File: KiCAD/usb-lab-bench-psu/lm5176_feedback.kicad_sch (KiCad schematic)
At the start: 17 parts, among them J10 Conn_01x03, U10 MCP602, U11 MCP4728

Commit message: restructured schematics to better show individual boards
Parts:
- renumbered J10 to J25, R62 to R100, R61 to R101, U10 to U17
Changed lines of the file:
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@@
 		(instances
 			(project "usb-lab-bench-psu"
-				(path "/63928bc9-e618-488a-a687-c6d5597f31d9/ef40a3f9-2fe8-4f01-b5d3-ede47a6064fc/25196ac8-3e62-4aeb-a723-5f08504eebf8"
-					(reference "R51")
+				(path "/63928bc9-e618-488a-a687-c6d5597f31d9/a793a91b-724b-4226-ba64-0dd946e3992c/7f670fa9-133d-4e8e-a284-e2ede26f8135/25196ac8-3e62-4aeb-a723-5f08504eebf8"
+					(reference "R92")
 					(unit 1)
 				)
@@
 		(dnp no)
 		(fields_autoplaced yes)
-		(property "Reference" "U10"
+		(property "Reference" "U17"
 			(at 86.36 59.6899 0)
 			(effects
@@
 		)
 		(instances
-			(project ""
-				(path "/63928bc9-e618-488a-a687-c6d5597f31d9/ef40a3f9-2fe8-4f01-b5d3-ede47a6064fc/25196ac8-3e62-4aeb-a723-5f08504eebf8"
-					(reference "U10")
+			(project "usb-lab-bench-psu"
+				(path "/63928bc9-e618-488a-a687-c6d5597f31d9/a793a91b-724b-4226-ba64-0dd946e3992c/7f670fa9-133d-4e8e-a284-e2ede26f8135/25196ac8-3e62-4aeb-a723-5f08504eebf8"
+					(reference "U17")
 					(unit 3)
 				)
@@
 		(instances
 			(project "usb-lab-bench-psu"
-				(path "/63928bc9-e618-488a-a687-c6d5597f31d9/ef40a3f9-2fe8-4f01-b5d3-ede47a6064fc/25196ac8-3e62-4aeb-a723-5f08504eebf8"
-					(reference "R57")
+				(path "/63928bc9-e618-488a-a687-c6d5597f31d9/a793a91b-724b-4226-ba64-0dd946e3992c/7f670fa9-133d-4e8e-a284-e2ede26f8135/25196ac8-3e62-4aeb-a723-5f08504eebf8"
+					(reference "R95")
 					(unit 1)
 				)
@@
 		(dnp no)
 		(fields_autoplaced yes)
-		(property "Reference" "J10"
+		(property "Reference" "J25"
 			(at 24.13 86.36 0)
 			(effects
@@
 		)
 		(instances
-			(project ""
-				(path "/63928bc9-e618-488a-a687-c6d5597f31d9/ef40a3f9-2fe8-4f01-b5d3-ede47a6064fc/25196ac8-3e62-4aeb-a723-5f08504eebf8"
-					(reference "J10")
+			(project "usb-lab-bench-psu"
+				(path "/63928bc9-e618-488a-a687-c6d5597f31d9/a793a91b-724b-4226-ba64-0dd946e3992c/7f670fa9-133d-4e8e-a284-e2ede26f8135/25196ac8-3e62-4aeb-a723-5f08504eebf8"
+					(reference "J25")
 					(unit 1)
 				)
@@
 		(dnp no)
 		(fields_autoplaced yes)
-		(property "Reference" "R61"
+		(property "Reference" "R101"
 			(at 191.77 60.96 90)
 			(effects
@@
 		)
 		(instances
-			(project ""
-				(path "/63928bc9-e618-488a-a687-c6d5597f31d9/ef40a3f9-2fe8-4f01-b5d3-ede47a6064fc/25196ac8-3e62-4aeb-a723-5f08504eebf8"
-					(reference "R61")
+			(project "usb-lab-bench-psu"
+				(path "/63928bc9-e618-488a-a687-c6d5597f31d9/a793a91b-724b-4226-ba64-0dd946e3992c/7f670fa9-133d-4e8e-a284-e2ede26f8135/25196ac8-3e62-4aeb-a723-5f08504eebf8"
+					(reference "R101")
 					(unit 1)
 				)
@@
 		(instances
 			(project "usb-lab-bench-psu"
-				(path "/63928bc9-e618-488a-a687-c6d5597f31d9/ef40a3f9-2fe8-4f01-b5d3-ede47a6064fc/25196ac8-3e62-4aeb-a723-5f08504eebf8"
-					(reference "R52")
+				(path "/63928bc9-e618-488a-a687-c6d5597f31d9/a793a91b-724b-4226-ba64-0dd946e3992c/7f670fa9-133d-4e8e-a284-e2ede26f8135/25196ac8-3e62-4aeb-a723-5f08504eebf8"
+					(reference "R93")
 					(unit 1)
 				)
@@
 		(instances
 			(project "usb-lab-bench-psu"
-				(path "/63928bc9-e618-488a-a687-c6d5597f31d9/ef40a3f9-2fe8-4f01-b5d3-ede47a6064fc/25196ac8-3e62-4aeb-a723-5f08504eebf8"
-					(reference "TP10")
+				(path "/63928bc9-e618-488a-a687-c6d5597f31d9/a793a91b-724b-4226-ba64-0dd946e3992c/7f670fa9-133d-4e8e-a284-e2ede26f8135/25196ac8-3e62-4aeb-a723-5f08504eebf8"
+					(reference "TP17")
 					(unit 1)
 				)
@@
 		(on_board yes)
 		(dnp no)
-		(property "Reference" "U10"
+		(property "Reference" "U17"
 			(at 199.39 91.44 0)
 			(effects
@@
 		)
 		(instances
-			(project ""
-				(path "/63928bc9-e618-488a-a687-c6d5597f31d9/ef40a3f9-2fe8-4f01-b5d3-ede47a6064fc/25196ac8-3e62-4aeb-a723-5f08504eebf8"
-					(reference "U10")
+			(project "usb-lab-bench-psu"
+				(path "/63928bc9-e618-488a-a687-c6d5597f31d9/a793a91b-724b-4226-ba64-0dd946e3992c/7f670fa9-133d-4e8e-a284-e2ede26f8135/25196ac8-3e62-4aeb-a723-5f08504eebf8"
+					(reference "U17")
 					(unit 1)
 				)
@@
 		(dnp no)
 		(fields_autoplaced yes)
-		(property "Reference" "U10"
+		(property "Reference" "U17"
 			(at 233.68 73.66 0)
 			(effects
@@
 		)
 		(instances
-			(project ""
-				(path "/63928bc9-e618-488a-a687-c6d5597f31d9/ef40a3f9-2fe8-4f01-b5d3-ede47a6064fc/25196ac8-3e62-4aeb-a723-5f08504eebf8"
-					(reference "U10")
+			(project "usb-lab-bench-psu"
+				(path "/63928bc9-e618-488a-a687-c6d5597f31d9/a793a91b-724b-4226-ba64-0dd946e3992c/7f670fa9-133d-4e8e-a284-e2ede26f8135/25196ac8-3e62-4aeb-a723-5f08504eebf8"
+					(reference "U17")
 					(unit 2)
 				)
@@
 		(instances
 			(project "usb-lab-bench-psu"
-				(path "/63928bc9-e618-488a-a687-c6d5597f31d9/ef40a3f9-2fe8-4f01-b5d3-ede47a6064fc/25196ac8-3e62-4aeb-a723-5f08504eebf8"
-					(reference "R58")
+				(path "/63928bc9-e618-488a-a687-c6d5597f31d9/a793a91b-724b-4226-ba64-0dd946e3992c/7f670fa9-133d-4e8e-a284-e2ede26f8135/25196ac8-3e62-4aeb-a723-5f08504eebf8"
+					(reference "R96")
 					(unit 1)
 				)
@@
 		(dnp no)
 		(fields_autoplaced yes)
-		(property "Reference" "R62"
+		(property "Reference" "R100"
 			(at 179.07 68.5799 0)
 			(effects
@@
 		)
 		(instances
-			(project ""
-				(path "/63928bc9-e618-488a-a687-c6d5597f31d9/ef40a3f9-2fe8-4f01-b5d3-ede47a6064fc/25196ac8-3e62-4aeb-a723-5f08504eebf8"
-					(reference "R62")
+			(project "usb-lab-bench-psu"
+				(path "/63928bc9-e618-488a-a687-c6d5597f31d9/a793a91b-724b-4226-ba64-0dd946e3992c/7f670fa9-133d-4e8e-a284-e2ede26f8135/25196ac8-3e62-4aeb-a723-5f08504eebf8"
+					(reference "R100")
 					(unit 1)
 				)
@@
 		(instances
 			(project "usb-lab-bench-psu"
-				(path "/63928bc9-e618-488a-a687-c6d5597f31d9/ef40a3f9-2fe8-4f01-b5d3-ede47a6064fc/25196ac8-3e62-4aeb-a723-5f08504eebf8"
-					(reference "R60")
+				(path "/63928bc9-e618-488a-a687-c6d5597f31d9/a793a91b-724b-4226-ba64-0dd946e3992c/7f670fa9-133d-4e8e-a284-e2ede26f8135/25196ac8-3e62-4aeb-a723-5f08504eebf8"
+					(reference "R99")
 					(unit 1)
 				)
@@
 		(instances
 			(project "usb-lab-bench-psu"
-				(path "/63928bc9-e618-488a-a687-c6d5597f31d9/ef40a3f9-2fe8-4f01-b5d3-ede47a6064fc/25196ac8-3e62-4aeb-a723-5f08504eebf8"
-					(reference "R64")
+				(path "/63928bc9-e618-488a-a687-c6d5597f31d9/a793a91b-724b-4226-ba64-0dd946e3992c/7f670fa9-133d-4e8e-a284-e2ede26f8135/25196ac8-3e62-4aeb-a723-5f08504eebf8"
+					(reference "R98")
 					(unit 1)
 				)
@@
 		(instances
 			(project "usb-lab-bench-psu"
-				(path "/63928bc9-e618-488a-a687-c6d5597f31d9/ef40a3f9-2fe8-4f01-b5d3-ede47a6064fc/25196ac8-3e62-4aeb-a723-5f08504eebf8"
-					(reference "R63")
+				(path "/63928bc9-e618-488a-a687-c6d5597f31d9/a793a91b-724b-4226-ba64-0dd946e3992c/7f670fa9-133d-4e8e-a284-e2ede26f8135/25196ac8-3e62-4aeb-a723-5f08504eebf8"
+					(reference "R97")
 					(unit 1)
 				)
@@
 		(instances
 			(project "usb-lab-bench-psu"
-				(path "/63928bc9-e618-488a-a687-c6d5597f31d9/ef40a3f9-2fe8-4f01-b5d3-ede47a6064fc/25196ac8-3e62-4aeb-a723-5f08504eebf8"
-					(reference "R56")
+				(path "/63928bc9-e618-488a-a687-c6d5597f31d9/a793a91b-724b-4226-ba64-0dd946e3992c/7f670fa9-133d-4e8e-a284-e2ede26f8135/25196ac8-3e62-4aeb-a723-5f08504eebf8"
+					(reference "R94")
 					(unit 1)
 				)
@@
 		(instances
 			(project "usb-lab-bench-psu"
-				(path "/63928bc9-e618-488a-a687-c6d5597f31d9/ef40a3f9-2fe8-4f01-b5d3-ede47a6064fc/25196ac8-3e62-4aeb-a723-5f08504eebf8"
-					(reference "TP11")
+				(path "/63928bc9-e618-488a-a687-c6d5597f31d9/a793a91b-724b-4226-ba64-0dd946e3992c/7f670fa9-133d-4e8e-a284-e2ede26f8135/25196ac8-3e62-4aeb-a723-5f08504eebf8"
+					(reference "TP18")
 					(unit 1)
 				)
@@
 		(instances
 			(project "usb-lab-bench-psu"
-				(path "/63928bc9-e618-488a-a687-c6d5597f31d9/ef40a3f9-2fe8-4f01-b5d3-ede47a6064fc/25196ac8-3e62-4aeb-a723-5f08504eebf8"
-					(reference "TP12")
+				(path "/63928bc9-e618-488a-a687-c6d5597f31d9/a793a91b-724b-4226-ba64-0dd946e3992c/7f670fa9-133d-4e8e-a284-e2ede26f8135/25196ac8-3e62-4aeb-a723-5f08504eebf8"
+					(reference "TP16")
 					(unit 1)
 				)
@@
 		(instances
 			(project "usb-lab-bench-psu"
-				(path "/63928bc9-e618-488a-a687-c6d5597f31d9/ef40a3f9-2fe8-4f01-b5d3-ede47a6064fc/25196ac8-3e62-4aeb-a723-5f08504eebf8"
-					(reference "R59")
+				(path "/63928bc9-e618-488a-a687-c6d5597f31d9/a793a91b-724b-4226-ba64-0dd946e3992c/7f670fa9-133d-4e8e-a284-e2ede26f8135/25196ac8-3e62-4aeb-a723-5f08504eebf8"
+					(reference "R91")
 					(unit 1)
 				)
@@
 		(instances
 			(project "usb-lab-bench-psu"
-				(path "/63928bc9-e618-488a-a687-c6d5597f31d9/ef40a3f9-2fe8-4f01-b5d3-ede47a6064fc/25196ac8-3e62-4aeb-a723-5f08504eebf8"
-					(reference "U11")
-					(unit 1)
-				)
+				(path "/63928bc9-e618-488a-a687-c6d5597f31d9/a793a91b-724b-4226-ba64-0dd946e3992c/7f670fa9-133d-4e8e-a284-e2ede26f8135/25196ac8-3e62-4aeb-a723-5f08504eebf8"
+					(reference "U16")
+					(unit 1)
+				)

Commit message: updated spi for display
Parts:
- renumbered R59 to R91, R51 to R92, R52 to R93, R56 to R94, R57 to R95, R58 to R96, R63 to R97, R64 to R98, R60 to R99, TP12 to TP16, TP10 to TP17, TP11 to TP18, U11 to U16
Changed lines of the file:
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@@
 		(on_board yes)
 		(dnp no)
-		(property "Reference" "R51"
+		(property "Reference" "R92"
 			(at 41.656 81.28 0)
 			(effects
@@
 		(on_board yes)
 		(dnp no)
-		(property "Reference" "R57"
+		(property "Reference" "R95"
 			(at 129.54 82.55 90)
 			(effects
@@
 		(dnp no)
 		(fields_autoplaced yes)
-		(property "Reference" "R52"
+		(property "Reference" "R93"
 			(at 53.34 81.2799 0)
 			(effects
@@
 		(dnp no)
 		(fields_autoplaced yes)
-		(property "Reference" "TP10"
+		(property "Reference" "TP17"
 			(at 135.89 79.2479 0)
 			(effects
@@
 		(on_board yes)
 		(dnp no)
-		(property "Reference" "R58"
+		(property "Reference" "R96"
 			(at 129.54 97.79 90)
 			(effects
@@
 		(dnp no)
 		(fields_autoplaced yes)
-		(property "Reference" "R60"
+		(property "Reference" "R99"
 			(at 170.18 41.91 90)
 			(effects
@@
 		(dnp no)
 		(fields_autoplaced yes)
-		(property "Reference" "R64"
+		(property "Reference" "R98"
 			(at 167.64 88.8999 0)
 			(effects
@@
 		(dnp no)
 		(fields_autoplaced yes)
-		(property "Reference" "R63"
+		(property "Reference" "R97"
 			(at 167.64 68.5799 0)
 			(effects
@@
 		(on_board yes)
 		(dnp no)
-		(property "Reference" "R56"
+		(property "Reference" "R94"
 			(at 116.84 96.52 90)
 			(effects
@@
 		(dnp no)
 		(fields_autoplaced yes)
-		(property "Reference" "TP11"
+		(property "Reference" "TP18"
 			(at 135.89 103.3779 0)
 			(effects
@@
 		(on_board yes)
 		(dnp no)
-		(property "Reference" "TP12"
+		(property "Reference" "TP16"
 			(at 90.932 77.216 0)
 			(effects
@@
 		(on_board yes)
 		(dnp no)
-		(property "Reference" "R59"
+		(property "Reference" "R91"
 			(at 27.686 82.55 0)
 			(effects
@@
 		(dnp no)
 		(fields_autoplaced yes)
-		(property "Reference" "U11"
+		(property "Reference" "U16"
 			(at 75.8541 82.55 0)
 			(effects

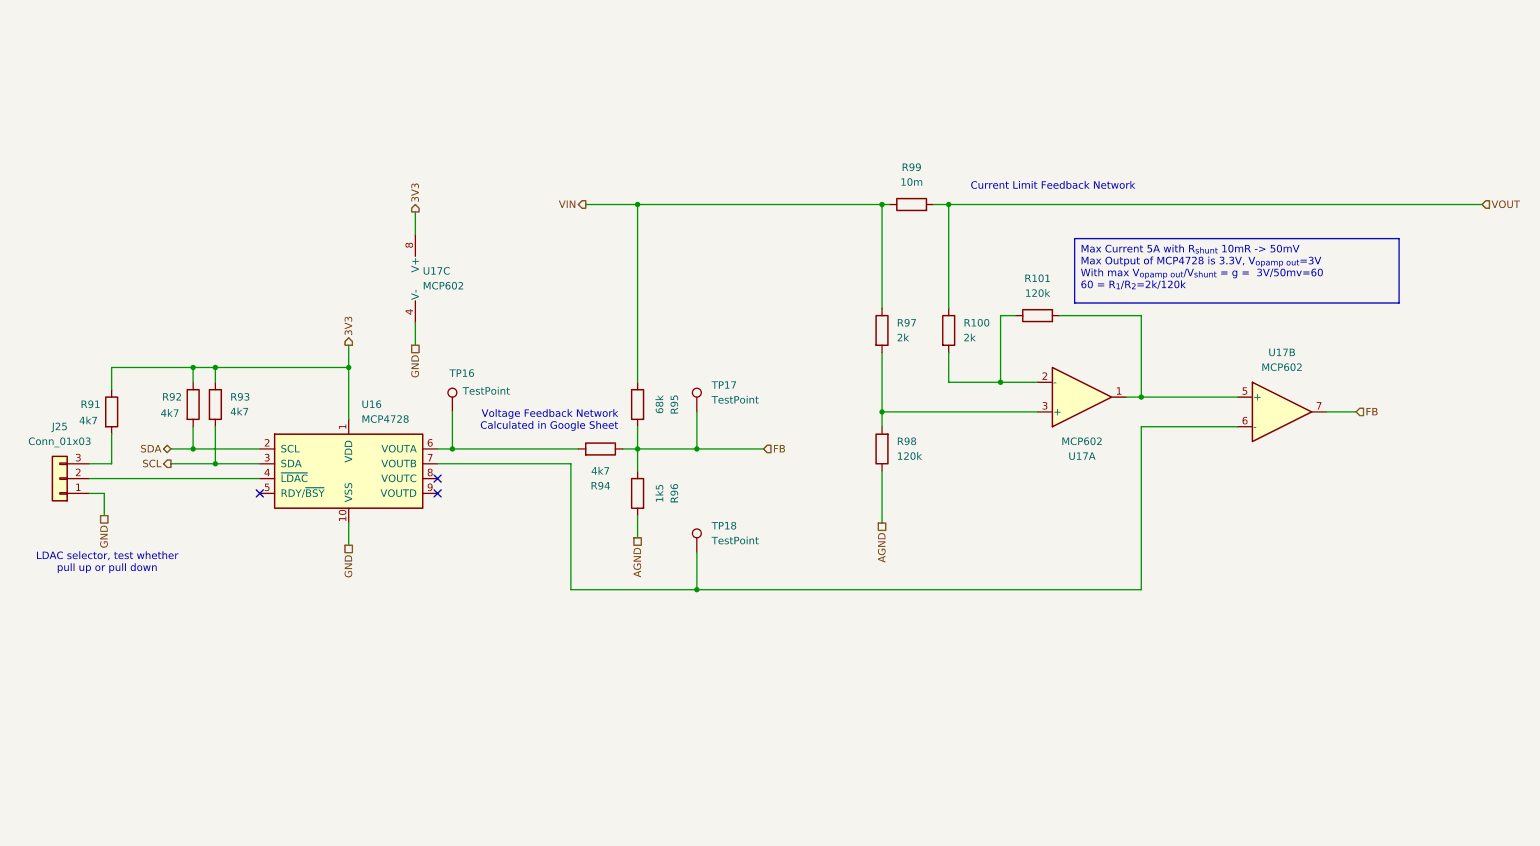
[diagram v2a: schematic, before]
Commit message: added current limiting circuit for USB PD sink, added 2nd buck converter
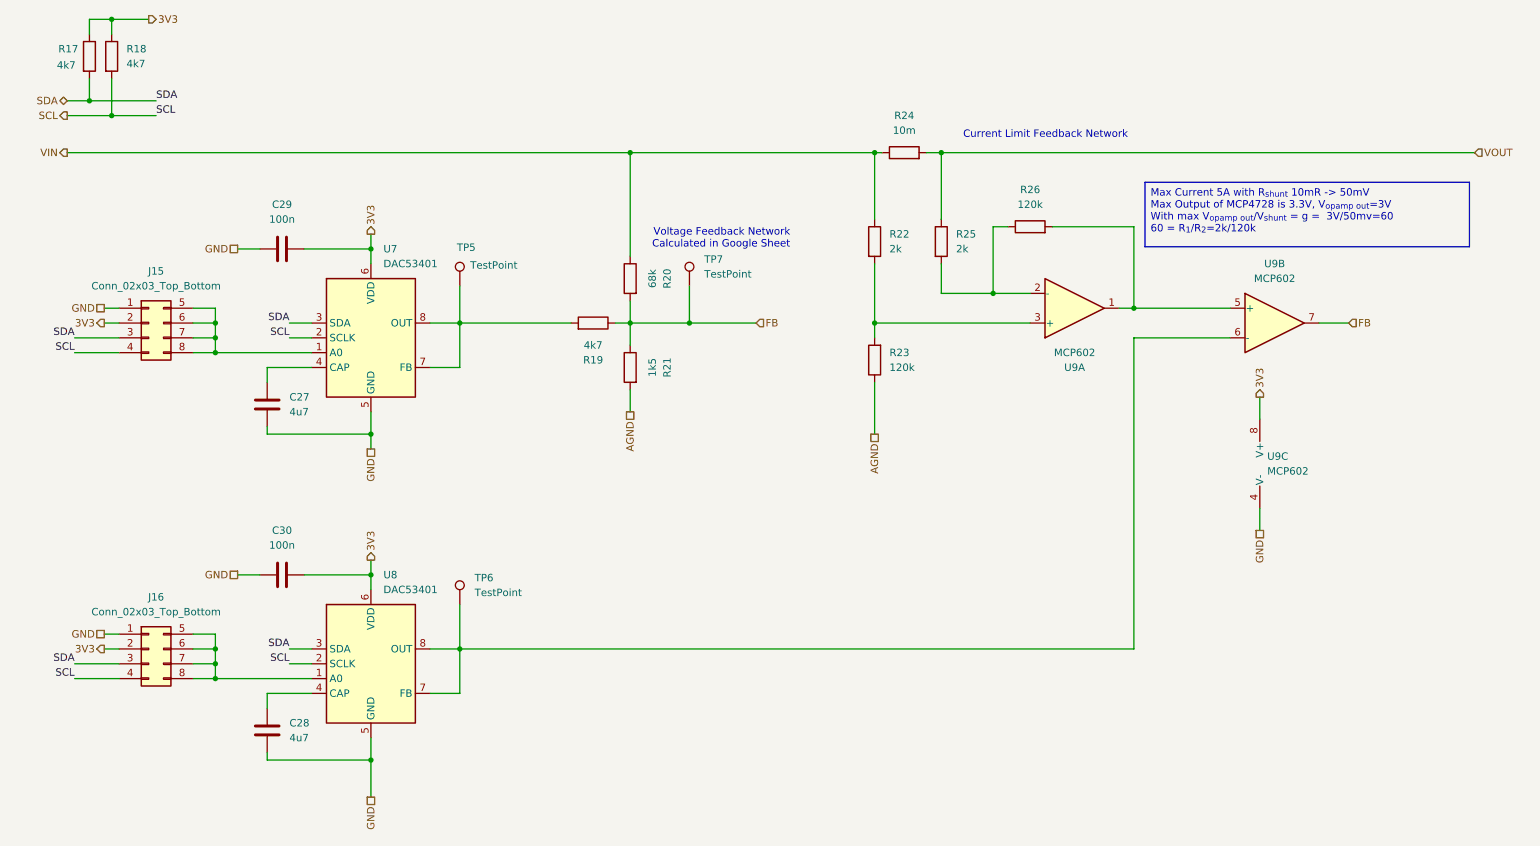
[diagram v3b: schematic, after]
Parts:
- removed J25: Conn_01x03, symbol Connector_Generic:Conn_01x03
- removed R91: 4k7, symbol Device:R
- removed U16: MCP4728, Package_SO:MSOP-10_3x3mm_P0.5mm, symbol Analog_DAC:MCP4728
- added C27, C28: 4u7, symbol Device:C
- added C29, C30: 100n, symbol Device:C
- added J15, J16: Conn_02x03_Top_Bottom, symbol Connector_Generic:Conn_02x04_Top_Bottom
- added U7, U8: DAC53401, Package_SON:WSON-8-1EP_2x2mm_P0.5mm_EP0.9x1.6mm, symbol Prj_DAC:DAC53401
- renumbered R92 to R17, R93 to R18, R94 to R19, R95 to R20, R96 to R21, R97 to R22, R98 to R23, R99 to R24, R100 to R25, R101 to R26, TP16 to TP5, TP18 to TP6, TP17 to TP7, U17 to U9
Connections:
- net 3V3: now also C29.1, C30.1, J15.2 (Pin_2), J16.2 (Pin_2), U7.6 (VDD), U8.6 (VDD)
- net GND: now also C27.2, C28.2, C29.2, C30.2, J15.1 (Pin_1), J16.1 (Pin_1), U7.5 (GND), U8.5 (GND)
- net SCL: now also J15.4 (Pin_4), J16.4 (Pin_4), U7.2 (SCLK), U8.2 (SCLK)
- net SDA: now also J15.3 (Pin_3), J16.3 (Pin_3), U7.3 (SDA), U8.3 (SDA)
- net at TP6.1, U9.6 (-): now also U8.7 (FB), U8.8 (OUT)
- net at R19.2, TP5.1: now also U7.7 (FB), U7.8 (OUT)
- new net: J16.5 (Pin_5), J16.6 (Pin_6), J16.7 (Pin_7), J16.8 (Pin_8), U8.1 (A0)
- new net: C28.1, U8.4 (CAP)
- new net: C27.1, U7.4 (CAP)
- new net: J15.5 (Pin_5), J15.6 (Pin_6), J15.7 (Pin_7), J15.8 (Pin_8), U7.1 (A0)
- no-connect marks 3 -> 0
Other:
- note removed: "LDAC selector, test whether pull up or pull down"
- moved on the sheet: R17, R18, R19, R20, R21, R22, R23, R24, R25, R26, TP5, TP6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

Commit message: Fixed label directions
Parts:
- removed R17, R18: 4k7, symbol Device:R
